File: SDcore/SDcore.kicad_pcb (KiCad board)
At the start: 4 copper layers, 24 x 32 mm, 44 parts, among them J1 SD_Card_Device, Q1 L2N7002WT1G, U1 RP2350A_C42411118, U2 NMUX27518EPWJ, U3 W25Q128JVEIQ_TR, X1 ABM8-272-T3_C20625731

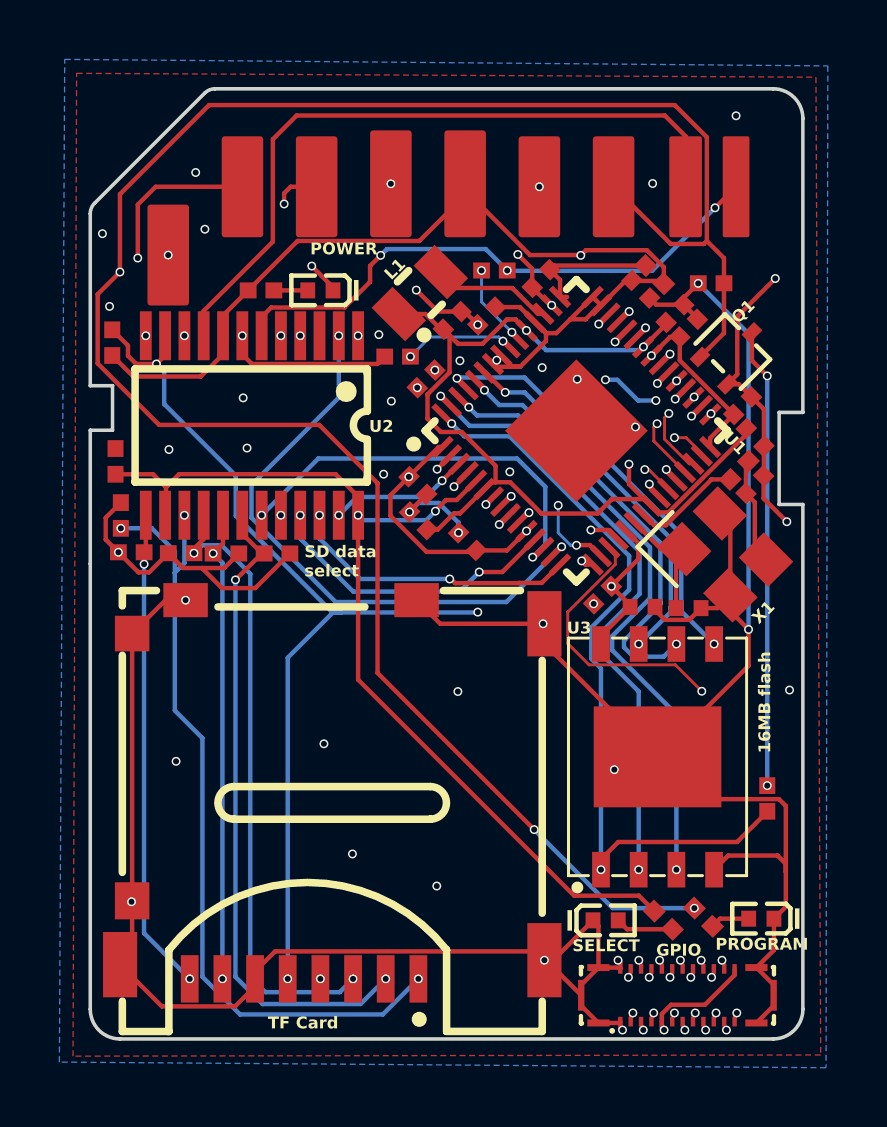
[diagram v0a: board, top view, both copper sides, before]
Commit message: Frogot to update board thickness
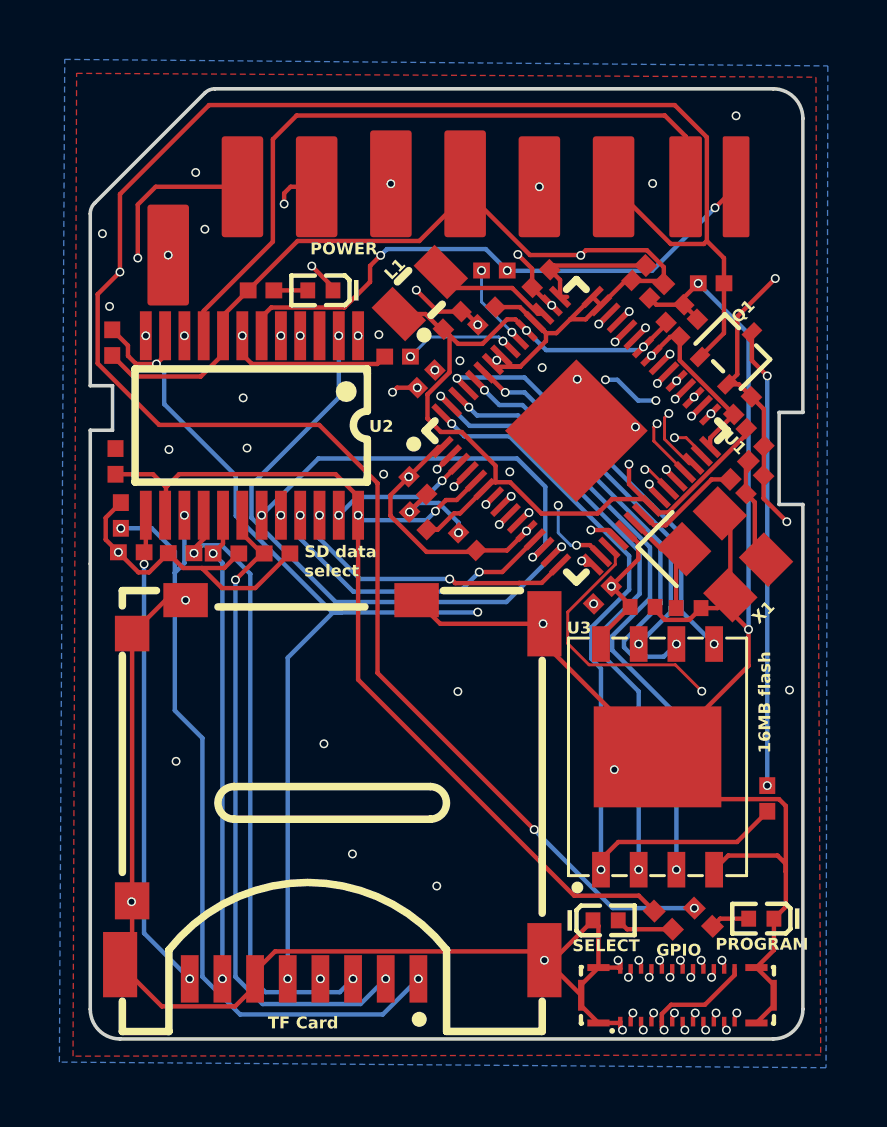
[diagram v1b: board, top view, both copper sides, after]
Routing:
- net GND: track 150.1 -> 150.7 mm
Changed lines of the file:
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@@
 	(generator_version "9.0")
 	(general
-		(thickness 1)
+		(thickness 0.8)
 		(legacy_teardrops no)
 	)
@@
 			(layer "dielectric 2"
 				(type "core")
-				(thickness 0.64)
+				(thickness 0.44)
 				(material "FR4")
 				(epsilon_r 4.5)
@@
 				(polygon
 					(pts
-						(xy 179.817909 88.233895) (xy 179.79402 88.206078) (xy 179.778956 88.180253) (xy 179.77113 88.155854)
-						(xy 179.769586 88.132206) (xy 179.77403 88.108701) (xy 179.78485 88.083135) (xy 179.803388 88.054823)
-						(xy 179.831467 88.023142) (xy 180.013602 87.841006) (xy 180.07063 87.898034) (xy 179.874177 88.094487)
-						(xy 179.861372 88.110016) (xy 179.854009 88.124888) (xy 179.851173 88.139528) (xy 179.852611 88.154261)
-						(xy 179.858514 88.168345) (xy 179.869531 88.182273) (xy 179.883471 88.193301) (xy 179.897555 88.199202)
-						(xy 179.912276 88.200632) (xy 179.926916 88.197795) (xy 179.941788 88.190432) (xy 179.957318 88.177627)
-						(xy 180.15377 87.981174) (xy 180.210815 88.038219) (xy 180.02868 88.220355) (xy 179.996497 88.248916)
-						(xy 179.968099 88.267549) (xy 179.942786 88.278231) (xy 179.919806 88.282425) (xy 179.901021 88.281731)
-						(xy 179.881789 88.277072) (xy 179.861738 88.268043) (xy 179.840538 88.253961)
+						(xy 179.817909 88.233896) (xy 179.79402 88.206079) (xy 179.778956 88.180254) (xy 179.77113 88.155855)
+						(xy 179.769586 88.132207) (xy 179.77403 88.108702) (xy 179.78485 88.083136) (xy 179.803388 88.054824)
+						(xy 179.831467 88.023143) (xy 180.013602 87.841007) (xy 180.07063 87.898035) (xy 179.874177 88.094488)
+						(xy 179.861372 88.110017) (xy 179.854009 88.124889) (xy 179.851173 88.139529) (xy 179.852611 88.154262)
+						(xy 179.858514 88.168346) (xy 179.869531 88.182274) (xy 179.883471 88.193302) (xy 179.897555 88.199203)
+						(xy 179.912276 88.200633) (xy 179.926916 88.197796) (xy 179.941788 88.190433) (xy 179.957318 88.177628)
+						(xy 180.15377 87.981175) (xy 180.210815 88.03822) (xy 180.02868 88.220356) (xy 179.996497 88.248917)
+						(xy 179.968099 88.26755) (xy 179.942786 88.278232) (xy 179.919806 88.282426) (xy 179.901021 88.281732)
+						(xy 179.881789 88.277073) (xy 179.861738 88.268044) (xy 179.840538 88.253962)
 					)
 				)
 				(polygon
 					(pts
-						(xy 180.02925 88.33346) (xy 180.093047 88.397257) (xy 180.272661 88.217643) (xy 180.18237 88.221305)
-						(xy 180.183528 88.166021) (xy 180.331847 88.159251) (xy 180.38694 88.214344) (xy 180.148537 88.452748)
-						(xy 180.212352 88.516562) (xy 180.162078 88.566837) (xy 179.978975 88.383734)
+						(xy 180.02925 88.333461) (xy 180.093047 88.397258) (xy 180.272661 88.217644) (xy 180.18237 88.221306)
+						(xy 180.183528 88.166022) (xy 180.331847 88.159252) (xy 180.38694 88.214345) (xy 180.148537 88.452749)
+						(xy 180.212352 88.516563) (xy 180.162078 88.566838) (xy 179.978975 88.383735)
 					)
 				)
@@
 	)
 	(segment
+		(start 168.683015 86.366985)
+		(end 168.53 86.52)
+		(width 0.15)
+		(layer "F.Cu")
+		(net 2)
+	)
+	(segment
 		(start 181.036985 89.323015)
 		(end 181.026985 89.333015)
@@
 	)
 	(segment
+		(start 169.363015 86.366985)
+		(end 168.683015 86.366985)
+		(width 0.15)
+		(layer "F.Cu")
+		(net 2)
+	)
+	(segment
 		(start 179.36 102.6)
 		(end 179.836013 102.123987)
@@
 	)
 	(via
+		(at 168.53 86.52)
+		(size 0.3)
+		(drill 0.2)
+		(layers "F.Cu" "B.Cu")
+		(free yes)
+		(net 2)
+	)
+	(via
 		(at 170.8 85.46)
 		(size 0.3)
@@
 	)
 	(via
-		(at 168.49 86.82)
-		(size 0.3)
-		(drill 0.2)
-		(layers "F.Cu" "B.Cu")
-		(free yes)
-		(net 2)
-	)
-	(via
 		(at 161 88.45)
 		(size 0.3)
@@
 	)
 	(segment
-		(start 168.49 86.82)
-		(end 168.696898 86.82)
-		(width 0.15)
-		(layer "In1.Cu")
-		(net 2)
-	)
-	(segment
 		(start 174.75 86.08)
 		(end 174.75 84.4517)
@@
 		(width 0.15)
 		(layer "In1.Cu")
-		(net 2)
-	)
-	(segment
-		(start 168.696898 86.82)
-		(end 168.803449 86.926551)
-		(width 0.15)
-		(layer "In1.Cu")
